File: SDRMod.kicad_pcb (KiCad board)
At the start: 2 copper layers, 36 parts, among them P1 CONN_02X06, Q1 Q_NPN_BCE, U1 AX5043, U2 74LVC125, U3 74LVC125, Y1 Crystal

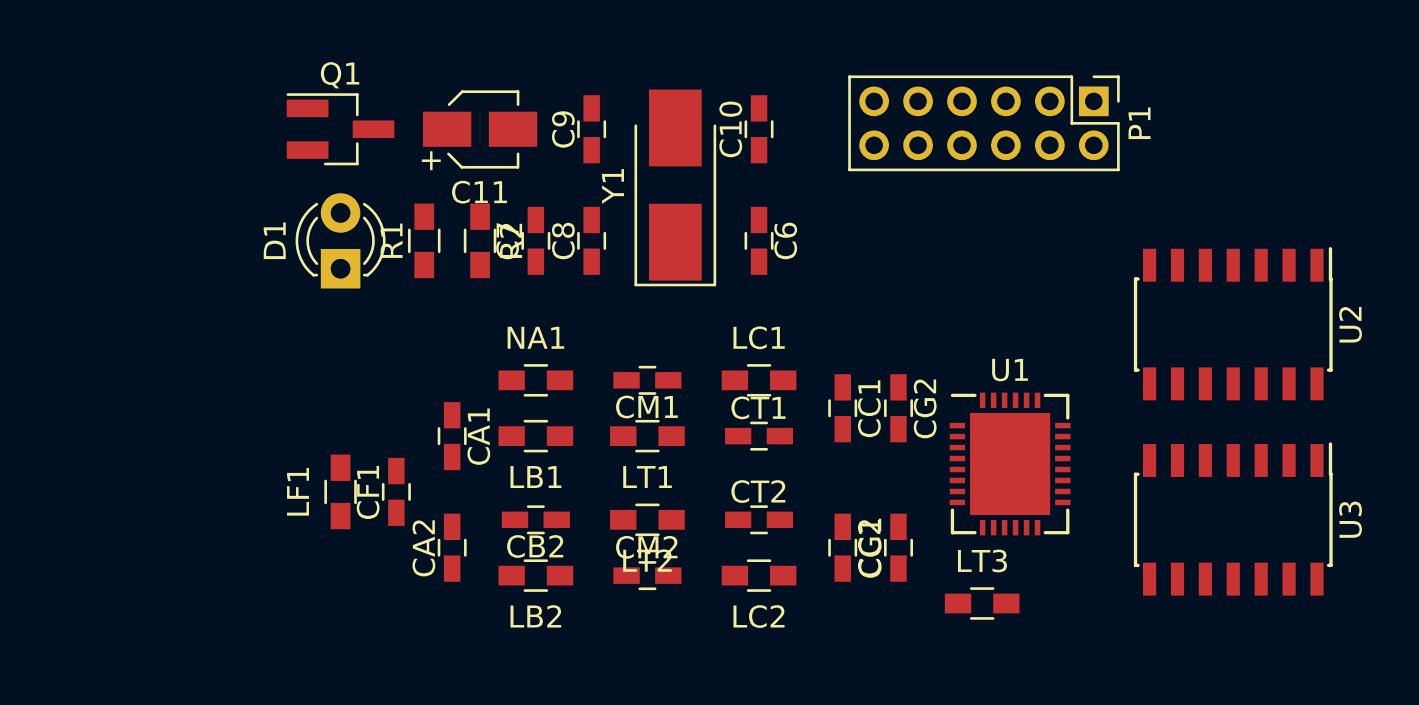
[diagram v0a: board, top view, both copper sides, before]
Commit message: the correct project uploaded (with FET based level shifters)
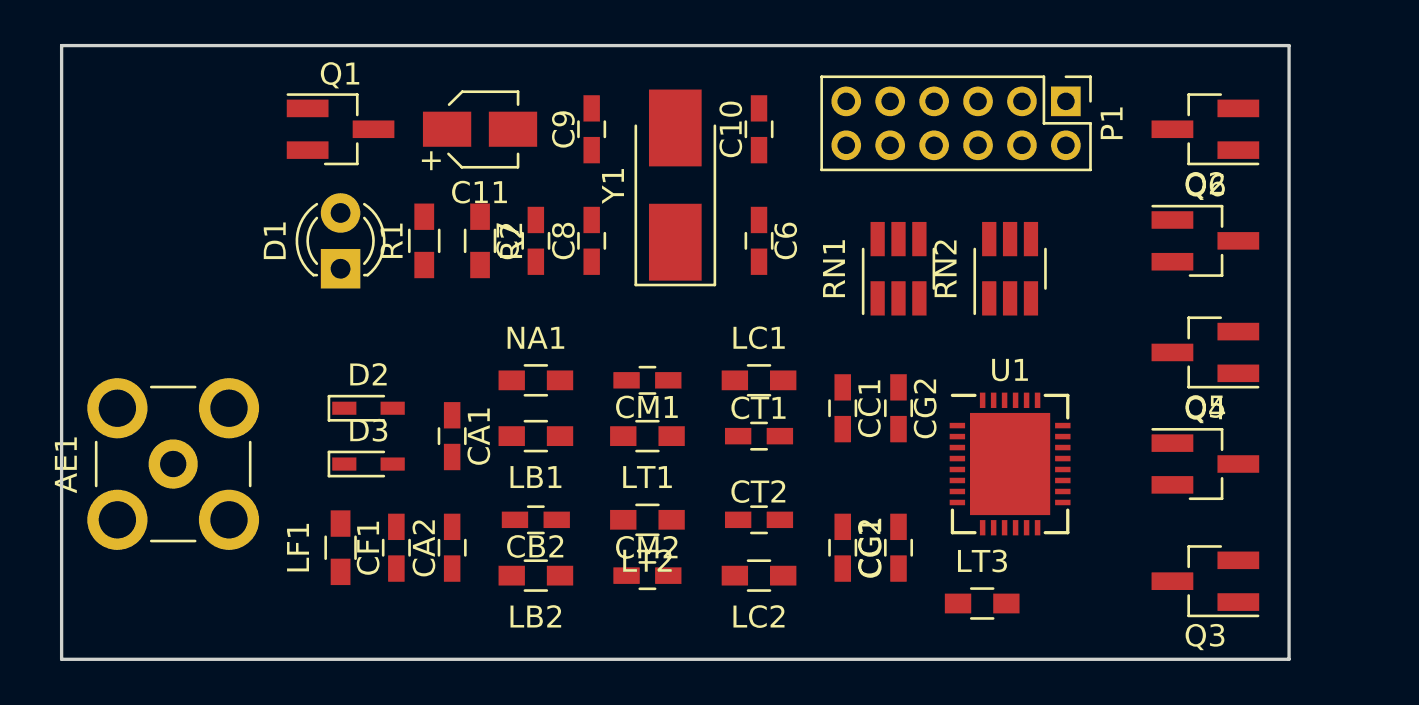
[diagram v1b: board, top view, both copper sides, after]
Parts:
- removed U2, U3: 74LVC125, Housings_SOIC:SOIC-14_3.9x8.7mm_Pitch1.27mm
- added AE1: Antenna_Shield, Connectors:SMB_Straight, F.Cu at (134.6, 123.2)
- added D2: BAV99, Diodes_SMD:D_SCD80_HandSoldering, F.Cu at (143.5, 120.7)
- added D3: BAV99, Diodes_SMD:D_SCD80_HandSoldering, F.Cu at (143.5, 123.2)
- added Q2: RE1C002UNTCL, TO_SOT_Packages_SMD:SOT-23_Handsoldering, F.Cu at (181.6, 108.0)
- added Q3: RE1C002UNTCL, TO_SOT_Packages_SMD:SOT-23_Handsoldering, F.Cu at (181.6, 128.5)
- added Q4: RE1C002UNTCL, TO_SOT_Packages_SMD:SOT-23_Handsoldering, F.Cu at (181.6, 123.2)
- added Q5: RE1C002UNTCL, TO_SOT_Packages_SMD:SOT-23_Handsoldering, F.Cu at (181.6, 118.1)
- added Q6: RE1C002UNTCL, TO_SOT_Packages_SMD:SOT-23_Handsoldering, F.Cu at (181.6, 113.0)
- added RN1: R_Network05, TO_SOT_Packages_SMD:SOT-23-6_Handsoldering, F.Cu at (167.6, 114.3)
- added RN2: R_Network05, TO_SOT_Packages_SMD:SOT-23-6_Handsoldering, F.Cu at (172.7, 114.3)
- moved CF1 2.54 mm to (144.8, 127.0)
- moved LF1 2.54 mm to (142.2, 127.0)
- moved P1 1.27 mm to (175.3, 106.7)
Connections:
- C10 pad 1: +1V8 -> +3V3
- C11 pad 1: +1V8 -> +3V3
- C6 pad 1: +1V8 -> +3V3
- C9 pad 1: +1V8 -> +3V3
- P1 pad 4: +1V8 -> +3V3
- R1 pad 1: +1V8 -> +3V3
- U1 pad 20: Net-(TP5-Pad1) -> (no net)
- U1 pad 21: Net-(TP4-Pad1) -> (no net)
- U1 pad 23: +1V8 -> +3V3
- U1 pad 4: (no net) -> Net-(CC2-Pad1)
- U1 pad 5: Net-(CC2-Pad1) -> (no net)
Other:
- board outline added: 55.9 x 27.9 mm
